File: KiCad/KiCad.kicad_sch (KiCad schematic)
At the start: 10 parts, among them M1 FA-130, U1 ESP32-DEVKITC, U2 microSD-DIP-KIT, U4 BD65496MUV

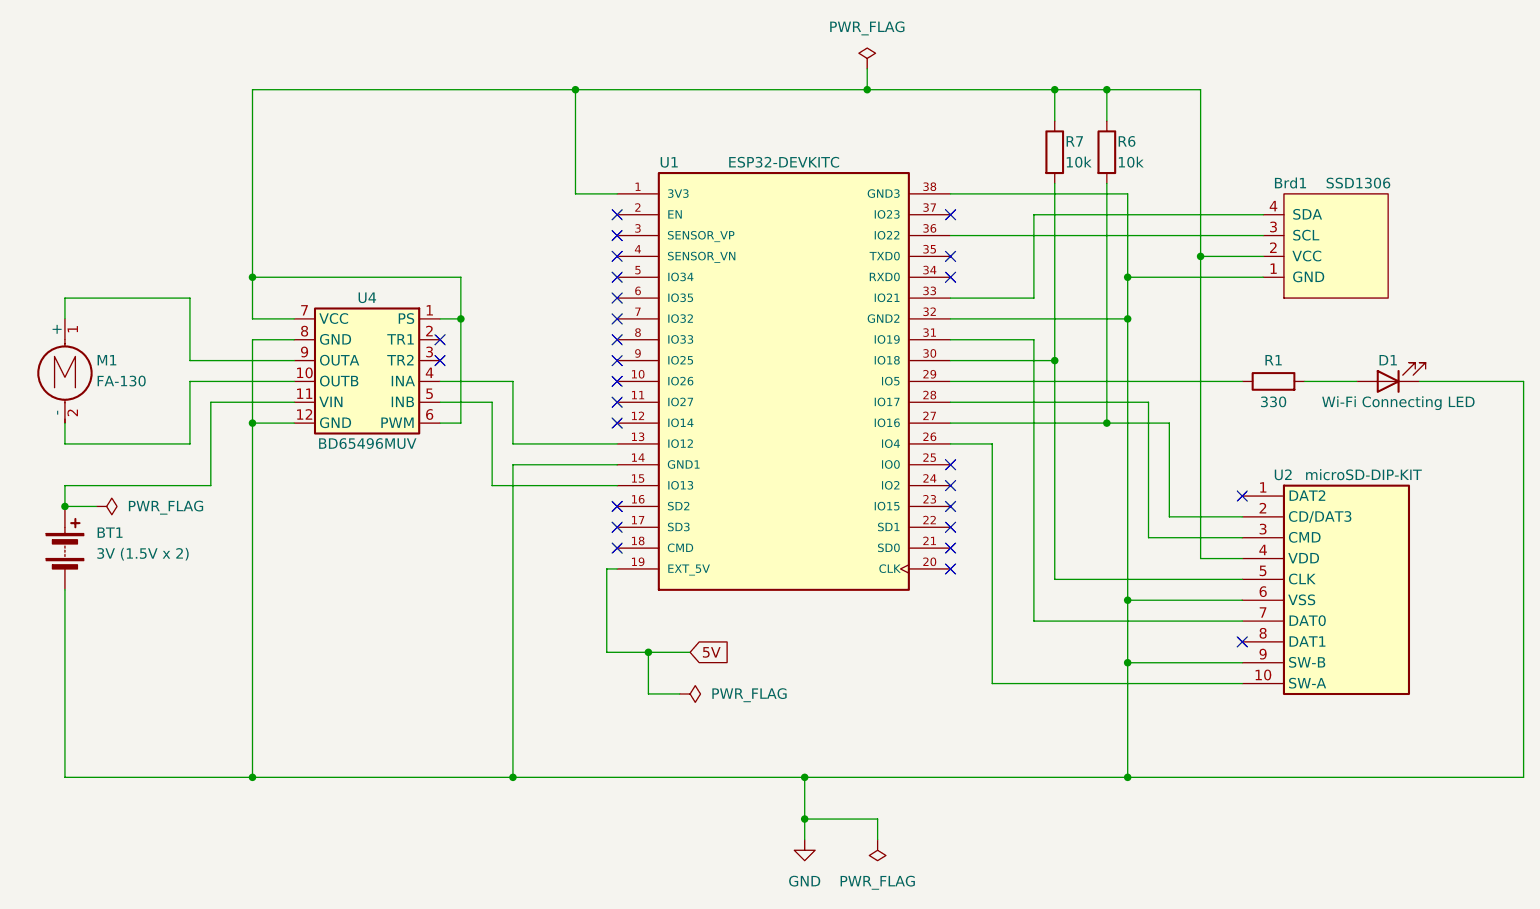
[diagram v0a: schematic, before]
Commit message: モーター2個に増量
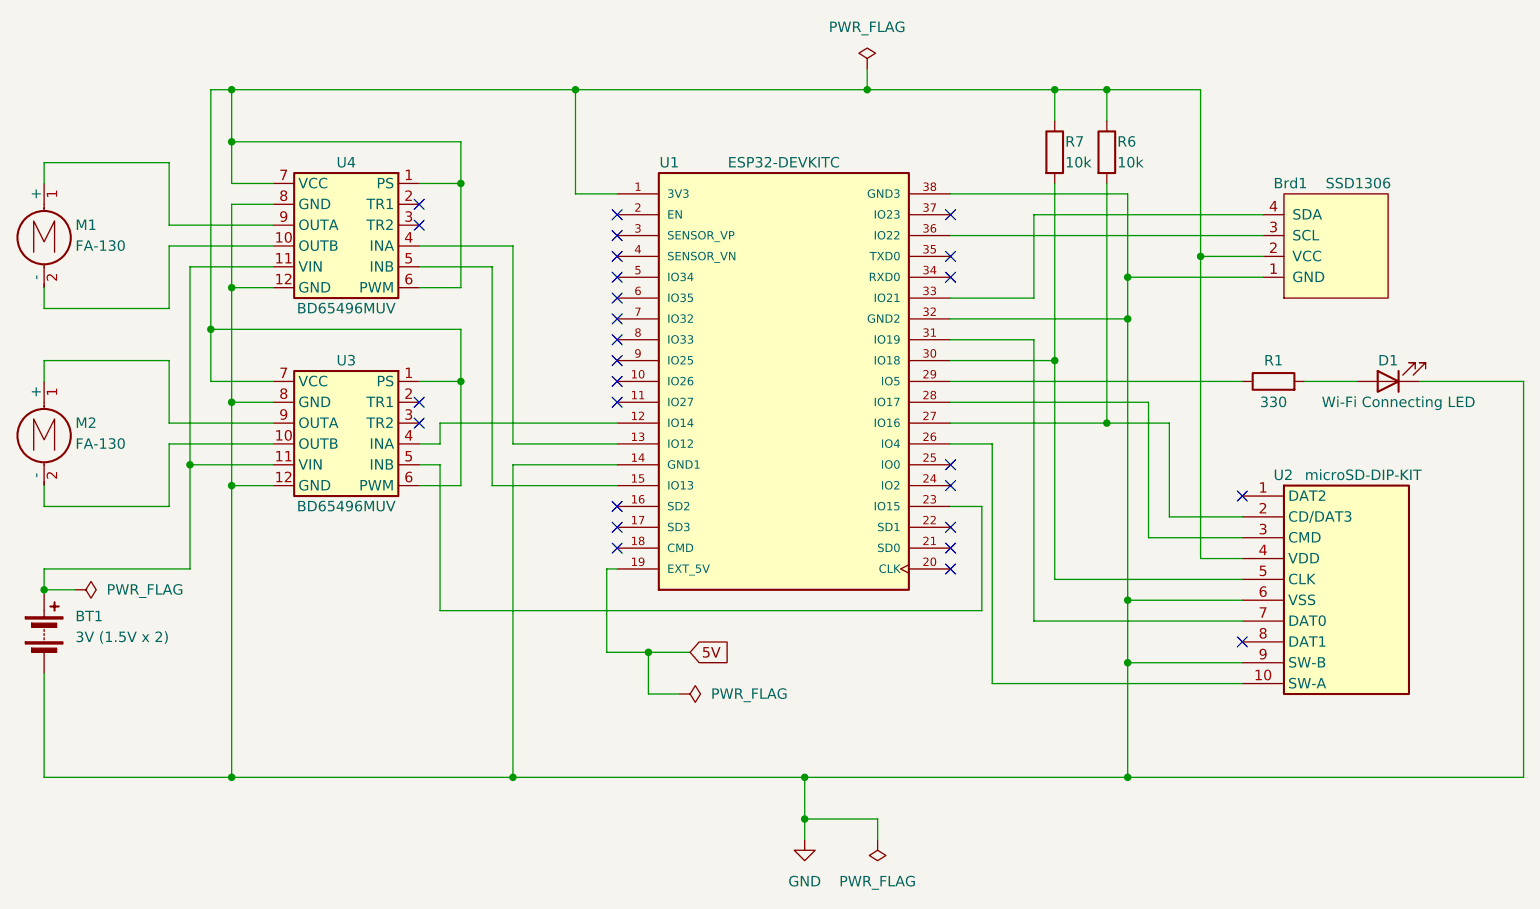
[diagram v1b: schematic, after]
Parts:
- added M2: FA-130, Connector_PinHeader_1.27mm:PinHeader_1x02_P1.27mm_Vertical, symbol Motor:Motor_DC
- added U3: BD65496MUV, SWITCH_SCIENCE:BD65496MUV, symbol SWITCH_SCIENCE_Library:BD65496MUV_Driver
- BT1, M1: footprint (none) -> Connector_PinHeader_1.27mm:PinHeader_1x02_P1.27mm_Vertical
- U4: footprint (none) -> SWITCH_SCIENCE:BD65496MUV
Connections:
- net GND: now also U3.12 (GND), U3.8 (GND)
- net at Brd1.2 (VCC), R6.1, R7.1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: now also U3.1 (PS), U3.6 (PWM), U3.7 (VCC)
- net at BT1.1 (+), U4.11 (VIN): now also U3.11 (VIN)
- net at U1.12 (IO14): now also U3.4 (INA)
- net at U1.23 (IO15): now also U3.5 (INB)
- new net: M2.1 (+), U3.9 (OUTA)
- new net: M2.2 (-), U3.10 (OUTB)
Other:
- moved on the sheet: BT1, M1, U4
